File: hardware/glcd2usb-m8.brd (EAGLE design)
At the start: 53 x 25.4 mm, 19 parts, among them IC1 MEGA8-P, Q1 12MHz, T1 BC547

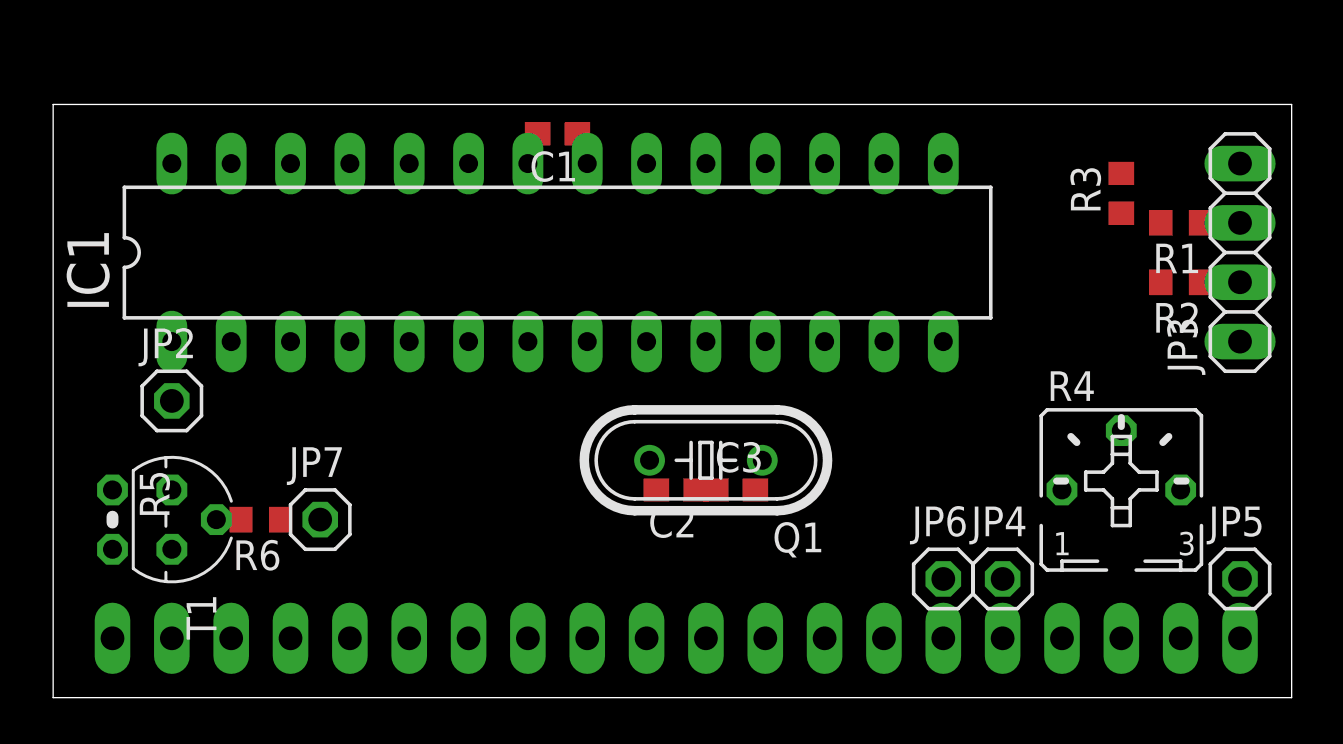
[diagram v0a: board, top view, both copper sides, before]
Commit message: use PortC for contntrol (glcd lib limitations)
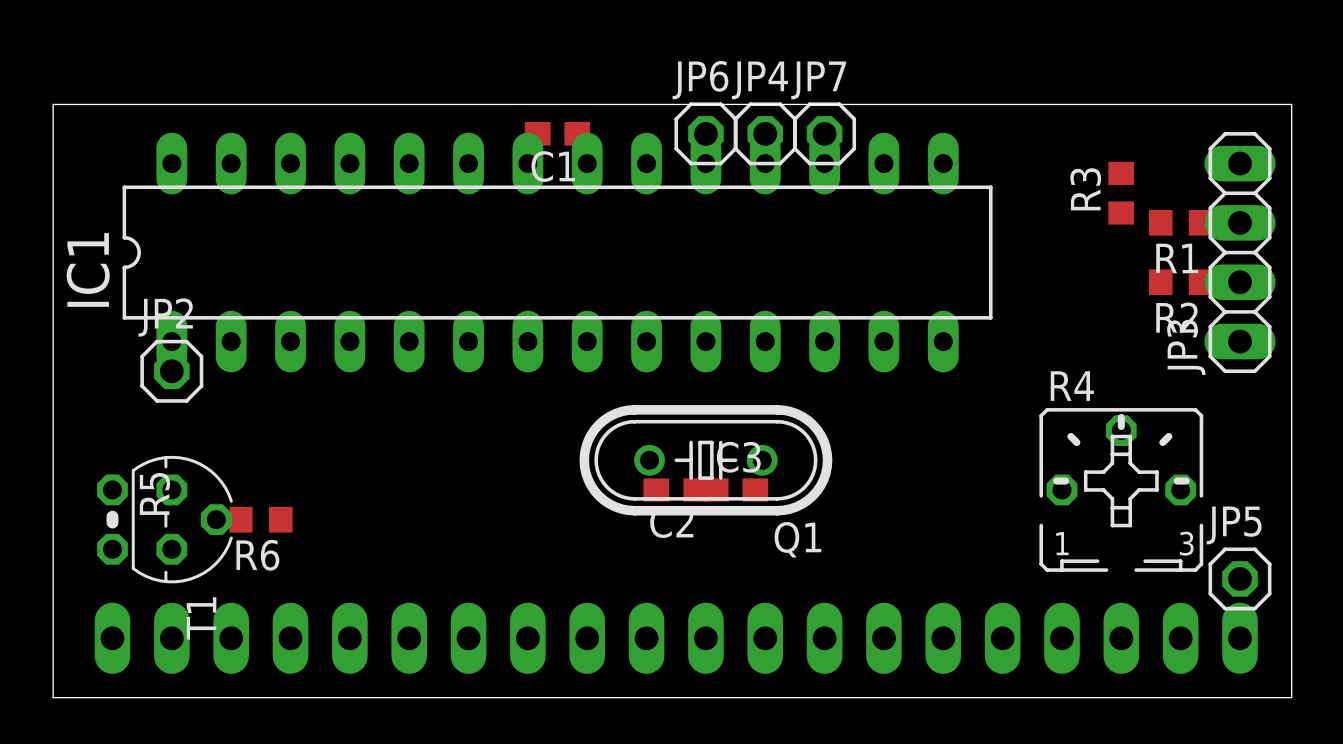
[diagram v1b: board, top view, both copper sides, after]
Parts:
- moved JP7 27.2 mm to (33.0, 24.1)
- moved JP4 21.6 mm to (30.5, 24.1)
- moved JP6 21.6 mm to (27.9, 24.1)
- moved JP2 1.27 mm to (5.08, 14.0)
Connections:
- new net MISO: IC1.18, JP4.1
- new net MOSI: JP6.1
- new net SCK: IC1.19
- net D/I: now also IC1.23; no longer IC1.16
- net E: now also IC1.25; no longer IC1.19, JP6.1
- net R/W: now also IC1.24; no longer IC1.18, JP4.1
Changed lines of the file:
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@@
 <element name="C3" library="resistor" package="C0603" value="22" x="29.21" y="8.89"/>
 <element name="JP1" library="pinhead" package="1X20" value="" x="26.67" y="2.54" rot="MR0"/>
-<element name="JP2" library="pinhead" package="1X01" value="!RESET" x="5.08" y="12.7"/>
-<element name="JP4" library="pinhead" package="1X01" value="MISO" x="40.64" y="5.08"/>
+<element name="JP2" library="pinhead" package="1X01" value="!RESET" x="5.08" y="13.97"/>
+<element name="JP4" library="pinhead" package="1X01" value="MISO" x="30.48" y="24.13"/>
 <element name="JP5" library="pinhead" package="1X01" value="GND" x="50.8" y="5.08"/>
-<element name="JP6" library="pinhead" package="1X01" value="SCK" x="38.1" y="5.08"/>
-<element name="JP7" library="pinhead" package="1X01" value="MOSI" x="11.43" y="7.62"/>
+<element name="JP6" library="pinhead" package="1X01" value="SCK" x="27.94" y="24.13"/>
+<element name="JP7" library="pinhead" package="1X01" value="MOSI" x="33.02" y="24.13"/>
 </elements>
 <signals>
@@
 <contactref element="IC1" pad="17"/>
 <contactref element="JP7" pad="1"/>
-<wire x1="11.43" y1="7.62" x2="33.02" y2="22.86" width="0" layer="19" extent="1-1"/>
-<wire x1="9.74" y1="7.62" x2="11.43" y2="7.62" width="0" layer="19" extent="1-1"/>
+<wire x1="33.02" y1="24.13" x2="33.02" y2="22.86" width="0" layer="19" extent="1-1"/>
+<wire x1="9.74" y1="7.62" x2="33.02" y2="22.86" width="0" layer="19" extent="1-1"/>
 </signal>
 <signal name="V0">
@@
 <signal name="E">
 <contactref element="JP1" pad="6"/>
-<contactref element="IC1" pad="19"/>
-<contactref element="JP6" pad="1"/>
-<wire x1="38.1" y1="5.08" x2="27.94" y2="22.86" width="0" layer="19" extent="1-1"/>
-<wire x1="38.1" y1="2.54" x2="38.1" y2="5.08" width="0" layer="19" extent="1-1"/>
+<contactref element="IC1" pad="25"/>
+<wire x1="12.7" y1="22.86" x2="38.1" y2="2.54" width="0" layer="19" extent="1-1"/>
 </signal>
 <signal name="D/I">
 <contactref element="JP1" pad="4"/>
-<contactref element="IC1" pad="16"/>
-<wire x1="43.18" y1="2.54" x2="35.56" y2="22.86" width="0" layer="19" extent="1-1"/>
+<contactref element="IC1" pad="23"/>
+<wire x1="17.78" y1="22.86" x2="43.18" y2="2.54" width="0" layer="19" extent="1-1"/>
 </signal>
 <signal name="R/W">
 <contactref element="JP1" pad="5"/>
-<contactref element="IC1" pad="18"/>
-<contactref element="JP4" pad="1"/>
-<wire x1="40.64" y1="5.08" x2="30.48" y2="22.86" width="0" layer="19" extent="1-1"/>
-<wire x1="40.64" y1="2.54" x2="40.64" y2="5.08" width="0" layer="19" extent="1-1"/>
+<contactref element="IC1" pad="24"/>
+<wire x1="15.24" y1="22.86" x2="40.64" y2="2.54" width="0" layer="19" extent="1-1"/>
 </signal>
 <signal name="CS1">
@@
 <contactref element="IC1" pad="1"/>
 <contactref element="JP2" pad="1"/>
-<wire x1="5.08" y1="12.7" x2="5.08" y2="15.24" width="0" layer="19" extent="1-1"/>
+<wire x1="5.08" y1="13.97" x2="5.08" y2="15.24" width="0" layer="19" extent="1-1"/>
 </signal>
 <signal name="D-">
@@
 <wire x1="49.11" y1="17.78" x2="50.8" y2="17.78" width="0" layer="19" extent="1-1"/>
 </signal>
+<signal name="MISO">
+<contactref element="IC1" pad="18"/>
+<contactref element="JP4" pad="1"/>
+<wire x1="30.48" y1="24.13" x2="30.48" y2="22.86" width="0" layer="19" extent="1-1"/>
+</signal>
+<signal name="SCK">
+<contactref element="IC1" pad="19"/>
+</signal>
+<signal name="MOSI">
+<contactref element="JP6" pad="1"/>
+</signal>
 </signals>

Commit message: fix connections
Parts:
- added IC2: LM1117-3.3, v-reg:SOT223
- R1, R2: value 220 -> 68; device resistor:R0603 -> resistor:0207/2V
- R3: value 10k -> 1k5; device resistor:R0603 -> resistor:0207/2V
- R6: device resistor:R0603 -> resistor:0207/2V
- moved R3 6.84 mm to (43.2, 15.2), turned to 0 degrees
- moved R6 1.27 mm to (10.2, 7.62)
- moved R1 1.27 mm to (47.0, 20.3)
- moved R2 1.27 mm to (47.0, 17.8)
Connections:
- removed net MOSI: JP6.1
- new net +5V: IC2.3, JP1.19, JP1.2, JP3.4, R4.E
- net GND: now also IC2.1
- net SCK: now also JP6.1
- net VCC: now also IC2.4; no longer JP1.19, JP1.2, JP3.4, R4.E
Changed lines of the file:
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@@
 </element>
 <element name="T1" library="transistor" package="TO92" value="BC547" x="5.08" y="7.62" rot="R270"/>
-<element name="R1" library="resistor" package="R0603" value="220" x="48.26" y="20.32" rot="R180"/>
-<element name="R2" library="resistor" package="R0603" value="220" x="48.26" y="17.78" rot="R180"/>
-<element name="R3" library="resistor" package="R0603" value="10k" x="45.72" y="21.59" rot="R90"/>
+<element name="R1" library="resistor" package="0207/2V" value="68" x="46.99" y="20.32" rot="R180"/>
+<element name="R2" library="resistor" package="0207/2V" value="68" x="46.99" y="17.78" rot="R180"/>
+<element name="R3" library="resistor" package="0207/2V" value="1k5" x="43.18" y="15.24"/>
 <element name="C1" library="resistor" package="C0603" value="" x="21.59" y="24.13" rot="R180"/>
 <element name="R4" library="pot" package="B25P" value="" x="45.72" y="8.89"/>
 <element name="R5" library="resistor" package="0204V" value="47" x="2.54" y="7.62" rot="R270"/>
-<element name="R6" library="resistor" package="R0603" value="4k7" x="8.89" y="7.62" rot="R180"/>
+<element name="R6" library="resistor" package="0207/2V" value="4k7" x="10.16" y="7.62" rot="R180"/>
 <element name="JP3" library="pinhead" package="1X04" value="USB" x="50.8" y="19.05" rot="R90"/>
 <element name="Q1" library="crystal" package="HC49/S" value="12MHz" x="27.94" y="10.16" rot="R180">
@@
 <element name="JP6" library="pinhead" package="1X01" value="SCK" x="27.94" y="24.13"/>
 <element name="JP7" library="pinhead" package="1X01" value="MOSI" x="33.02" y="24.13"/>
+<element name="IC2" library="v-reg" package="SOT223" value="LM1117-3.3" x="38.1" y="8.89"/>
 </elements>
 <signals>
@@
 <contactref element="IC1" pad="22"/>
 <contactref element="JP1" pad="1"/>
+<contactref element="JP5" pad="1"/>
+<contactref element="IC2" pad="1"/>
 <contactref element="C1" pad="2"/>
-<contactref element="JP5" pad="1"/>
 <wire x1="50.8" y1="5.08" x2="50.8" y2="15.24" width="0" layer="19" extent="1-1"/>
 <wire x1="50.8" y1="2.54" x2="50.8" y2="5.08" width="0" layer="19" extent="1-1"/>
-<wire x1="28.36" y1="8.89" x2="50.8" y2="5.08" width="0" layer="19" extent="1-1"/>
+<wire x1="35.8" y1="5.74" x2="50.8" y2="15.24" width="0" layer="19" extent="1-1"/>
+<wire x1="28.36" y1="8.89" x2="35.8" y2="5.74" width="0" layer="19" extent="1-1"/>
 <wire x1="27.52" y1="8.89" x2="28.36" y2="8.89" width="0" layer="19" extent="1-1"/>
 <wire x1="22.86" y1="15.24" x2="27.52" y2="8.89" width="0" layer="19" extent="1-1"/>
@@
 <signal name="VCC">
 <contactref element="IC1" pad="7"/>
-<contactref element="R3" pad="2"/>
-<contactref element="JP3" pad="4"/>
-<contactref element="R4" pad="E"/>
 <contactref element="IC1" pad="20"/>
 <contactref element="IC1" pad="21"/>
 <contactref element="IC1" pad="7"/>
-<contactref element="JP1" pad="19"/>
-<contactref element="JP1" pad="2"/>
 <contactref element="C1" pad="1"/>
-<wire x1="45.72" y1="22.44" x2="50.8" y2="22.86" width="0" layer="19" extent="1-1"/>
-<wire x1="48.26" y1="8.89" x2="45.72" y2="22.44" width="0" layer="19" extent="1-1"/>
-<wire x1="48.26" y1="2.54" x2="48.26" y2="8.89" width="0" layer="19" extent="1-1"/>
-<wire x1="25.4" y1="22.86" x2="45.72" y2="22.44" width="0" layer="19" extent="1-1"/>
-<wire x1="22.86" y1="22.86" x2="25.4" y2="22.86" width="0" layer="19" extent="1-1"/>
+<contactref element="IC2" pad="4"/>
+<contactref element="R3" pad="2"/>
+<wire x1="38.1" y1="12.04" x2="44.45" y2="15.24" width="0" layer="19" extent="1-1"/>
+<wire x1="20.32" y1="15.24" x2="38.1" y2="12.04" width="0" layer="19" extent="1-1"/>
+<wire x1="22.86" y1="22.86" x2="20.32" y2="15.24" width="0" layer="19" extent="1-1"/>
 <wire x1="22.44" y1="24.13" x2="22.86" y2="22.86" width="0" layer="19" extent="1-1"/>
-<wire x1="20.32" y1="15.24" x2="22.86" y2="22.86" width="0" layer="19" extent="1-1"/>
-<wire x1="5.08" y1="2.54" x2="20.32" y2="15.24" width="0" layer="19" extent="1-1"/>
+<wire x1="25.4" y1="22.86" x2="22.86" y2="22.86" width="0" layer="19" extent="1-1"/>
 </signal>
 <signal name="MD-">
@@
 <contactref element="IC1" pad="14"/>
 <contactref element="R3" pad="1"/>
-<wire x1="45.72" y1="20.74" x2="47.41" y2="20.32" width="0" layer="19" extent="1-1"/>
-<wire x1="38.1" y1="15.24" x2="45.72" y2="20.74" width="0" layer="19" extent="1-1"/>
+<wire x1="41.91" y1="15.24" x2="45.72" y2="20.32" width="0" layer="19" extent="1-1"/>
+<wire x1="38.1" y1="15.24" x2="41.91" y2="15.24" width="0" layer="19" extent="1-1"/>
 </signal>
 <signal name="MD+">
 <contactref element="R2" pad="2"/>
 <contactref element="IC1" pad="15"/>
-<wire x1="38.1" y1="22.86" x2="47.41" y2="17.78" width="0" layer="19" extent="1-1"/>
+<wire x1="38.1" y1="22.86" x2="45.72" y2="17.78" width="0" layer="19" extent="1-1"/>
 </signal>
 <signal name="D0">
@@
 <contactref element="T1" pad="2"/>
 <contactref element="R6" pad="2"/>
-<wire x1="6.985" y1="7.62" x2="8.04" y2="7.62" width="0" layer="19" extent="1-1"/>
+<wire x1="6.985" y1="7.62" x2="8.89" y2="7.62" width="0" layer="19" extent="1-1"/>
 </signal>
 <signal name="BL_PWM">
@@
 <contactref element="JP7" pad="1"/>
 <wire x1="33.02" y1="24.13" x2="33.02" y2="22.86" width="0" layer="19" extent="1-1"/>
-<wire x1="9.74" y1="7.62" x2="33.02" y2="22.86" width="0" layer="19" extent="1-1"/>
+<wire x1="11.43" y1="7.62" x2="33.02" y2="22.86" width="0" layer="19" extent="1-1"/>
 </signal>
 <signal name="V0">
@@
 <contactref element="R1" pad="1"/>
 <contactref element="JP3" pad="3"/>
-<wire x1="49.11" y1="20.32" x2="50.8" y2="20.32" width="0" layer="19" extent="1-1"/>
+<wire x1="48.26" y1="20.32" x2="50.8" y2="20.32" width="0" layer="19" extent="1-1"/>
 </signal>
 <signal name="D+">
 <contactref element="R2" pad="1"/>
 <contactref element="JP3" pad="2"/>
-<wire x1="49.11" y1="17.78" x2="50.8" y2="17.78" width="0" layer="19" extent="1-1"/>
+<wire x1="48.26" y1="17.78" x2="50.8" y2="17.78" width="0" layer="19" extent="1-1"/>
 </signal>
 <signal name="MISO">
@@
 <signal name="SCK">
 <contactref element="IC1" pad="19"/>
-</signal>
-<signal name="MOSI">
 <contactref element="JP6" pad="1"/>
+<wire x1="27.94" y1="24.13" x2="27.94" y2="22.86" width="0" layer="19" extent="1-1"/>
+</signal>
+<signal name="+5V">
+<contactref element="JP3" pad="4"/>
+<contactref element="IC2" pad="3"/>
+<contactref element="R4" pad="E"/>
+<contactref element="JP1" pad="2"/>
+<contactref element="JP1" pad="19"/>
+<wire x1="48.26" y1="8.89" x2="50.8" y2="22.86" width="0" layer="19" extent="1-1"/>
+<wire x1="48.26" y1="2.54" x2="48.26" y2="8.89" width="0" layer="19" extent="1-1"/>
+<wire x1="40.4" y1="5.74" x2="48.26" y2="8.89" width="0" layer="19" extent="1-1"/>
+<wire x1="5.08" y1="2.54" x2="40.4" y2="5.74" width="0" layer="19" extent="1-1"/>
 </signal>
 </signals>
